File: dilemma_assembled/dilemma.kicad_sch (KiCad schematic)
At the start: 103 parts, among them J1 USB_C_Receptacle_USB2.0, J102 NA_serial, J105 NA_Conn_01x04_Female, J113 Cirque, J2 NA_Conn_01x03_Female, J5 Conn_01x02, SW1 SW_Push, SW101 NA_SW_Push, SW102 NA_SW_Push, SW103 NA_SW_Push, SW104 NA_SW_Push, SW105 NA_SW_Push, SW106 NA_SW_Push, SW107 NA_SW_Push, SW108 NA_SW_Push, SW109 NA_SW_Push, SW110 NA_SW_SPST, SW112 NA_SW_Push, SW113 NA_SW_Push, SW114 NA_SW_Push, SW115 NA_SW_Push, SW116 NA_SW_Push, SW117 NA_SW_Push, SW118 NA_SW_Push, SW119 NA_SW_Push, SW2 SW_Push, SW3001 NA_SW_Push, SW3002 NA_RotaryEncoder_Switch, U1 RP2040, U2 W25Q128JVS, U3 XC6210B332MR-G, U4 USBLC6-2P6, Y1 Crystal_GND24

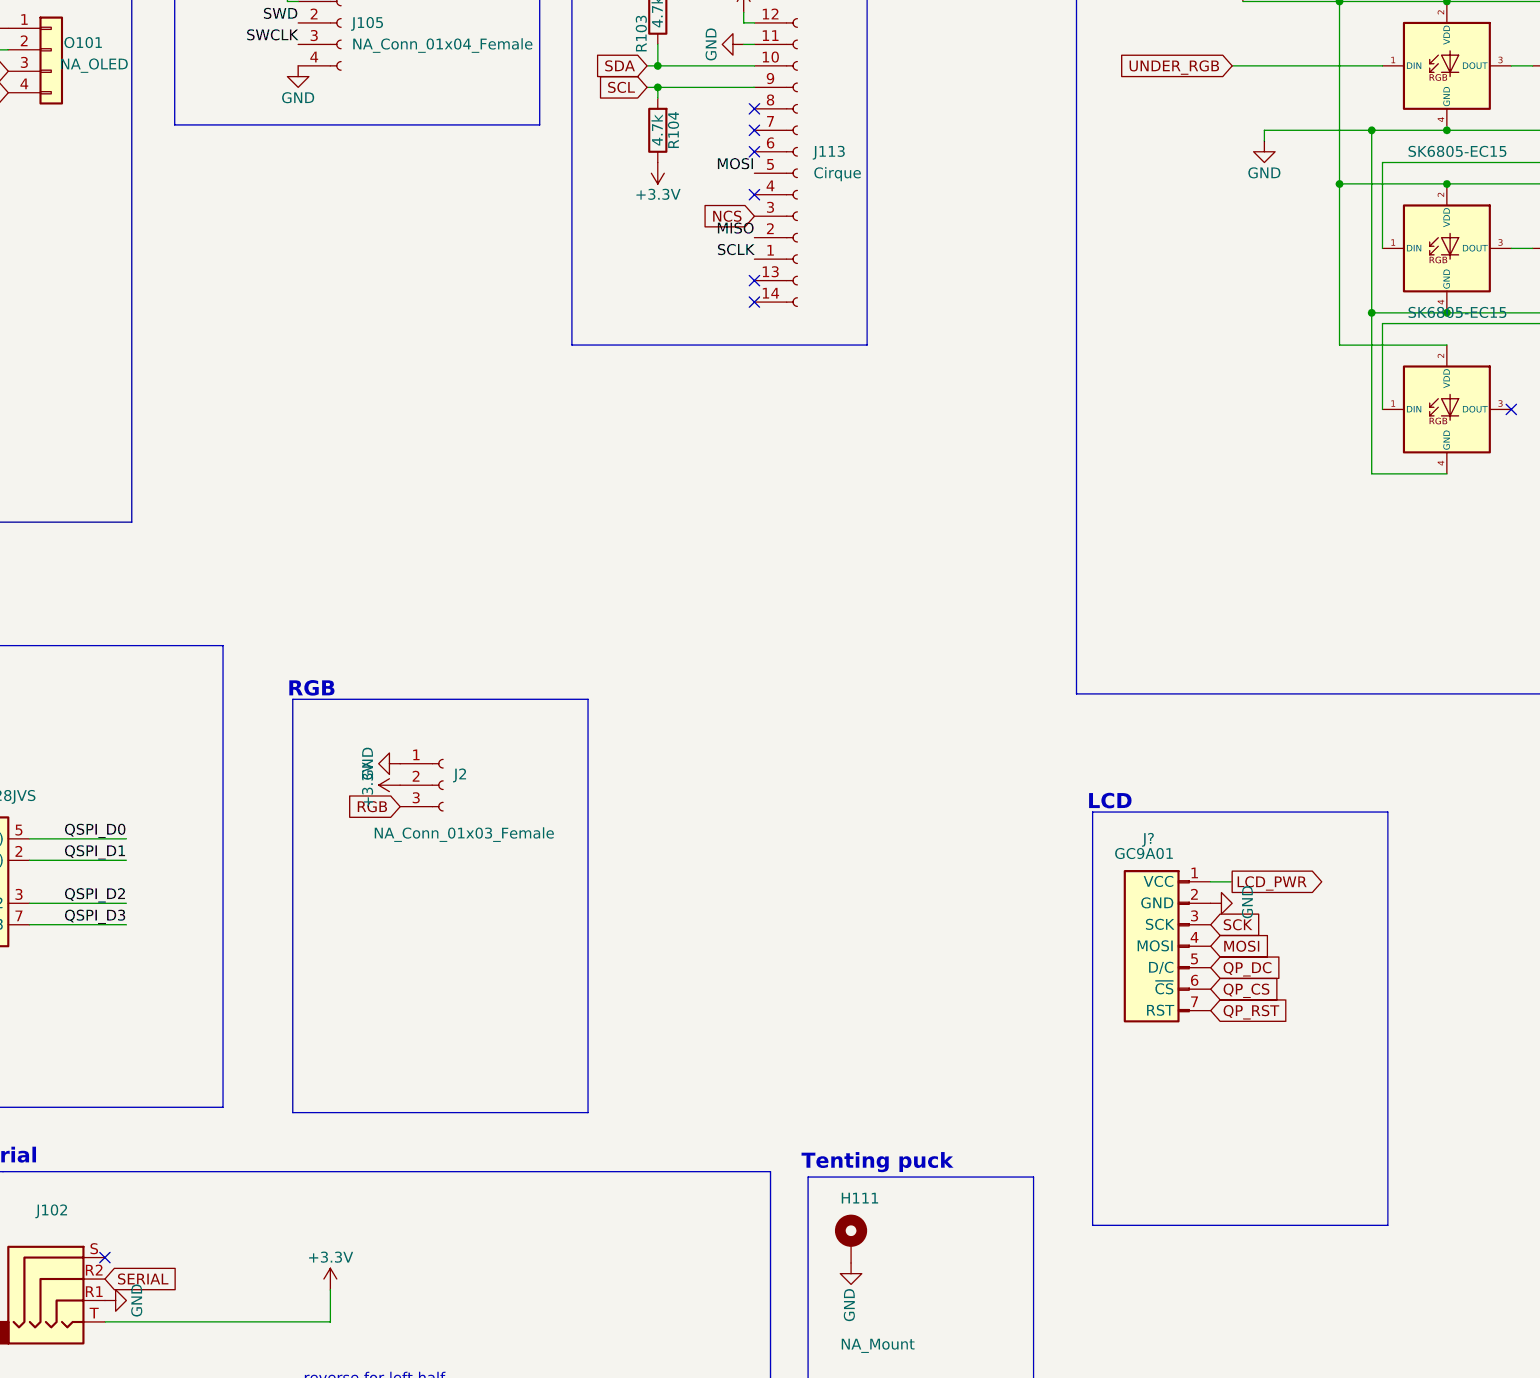
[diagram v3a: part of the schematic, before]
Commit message: add usb c cutout
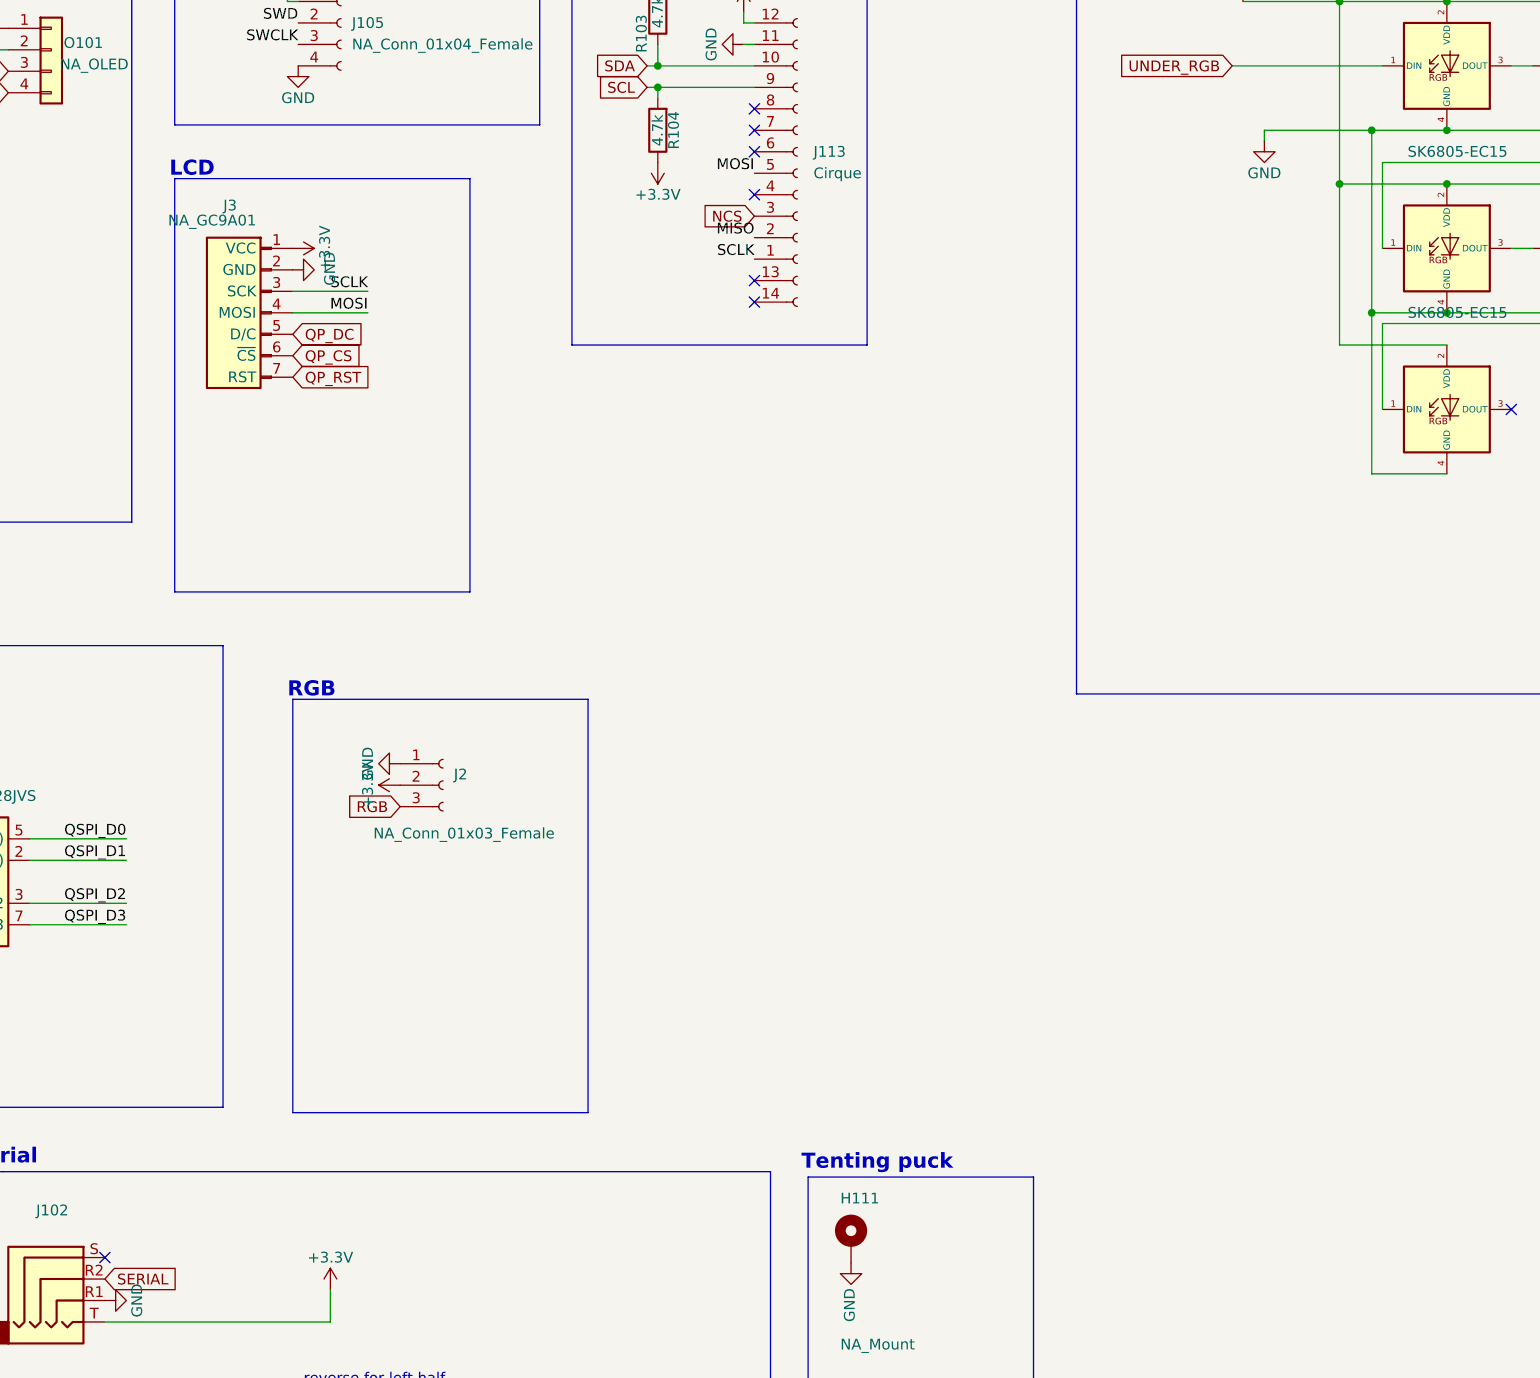
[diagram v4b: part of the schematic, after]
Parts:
- J3: renamed from J?; value GC9A01 -> NA_GC9A01; footprint prettylib:GC9A01-biggers hole -> Connector_PinHeader_2.54mm:PinHeader_1x07_P2.54mm_Vertical
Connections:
- net LCD_PWR is gone; now on net +3V3: J3.1 (VCC)
- net SCK is gone; now on net SCLK: J3.3 (SCK)
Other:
- moved on the sheet: J3
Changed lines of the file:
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@@
     (stroke (width 0) (type default) (color 0 0 0 0))
   )
-  (polyline (pts (xy 417.195 123.825) (xy 417.195 172.72))
+  (polyline (pts (xy 308.61 48.895) (xy 308.61 97.79))
     (stroke (width 0) (type default) (color 0 0 0 0))
   )
@@
     (stroke (width 0) (type default) (color 0 0 0 0))
   )
-  (wire (pts (xy 396.24 132.08) (xy 398.78 132.08))
-    (stroke (width 0) (type default) (color 0 0 0 0))
-  )
   (wire (pts (xy 64.135 44.45) (xy 64.135 45.085))
     (stroke (width 0) (type default) (color 0 0 0 0))
@@
     (stroke (width 0) (type default) (color 0 0 0 0))
   )
-  (polyline (pts (xy 382.27 123.825) (xy 382.27 172.72))
+  (polyline (pts (xy 273.685 48.895) (xy 273.685 97.79))
     (stroke (width 0) (type default) (color 0 0 0 0))
   )
@@
     (stroke (width 0) (type default) (color 0 0 0 0))
   )
-  (polyline (pts (xy 417.195 172.72) (xy 382.27 172.72))
+  (polyline (pts (xy 308.61 97.79) (xy 273.685 97.79))
     (stroke (width 0) (type default) (color 0 0 0 0))
   )
@@
     (stroke (width 0) (type default) (color 0 0 0 0))
   )
-  (polyline (pts (xy 382.27 123.825) (xy 417.195 123.825))
+  (polyline (pts (xy 273.685 48.895) (xy 308.61 48.895))
     (stroke (width 0) (type default) (color 0 0 0 0))
   )
@@
     (stroke (width 0) (type default) (color 0 0 0 0))
   )
+  (wire (pts (xy 287.655 64.77) (xy 296.545 64.77))
+    (stroke (width 0) (type default) (color 0 0 0 0))
+  )
   (wire (pts (xy 55.88 248.92) (xy 55.88 255.27))
     (stroke (width 0) (type default) (color 0 0 0 0))
@@
     (stroke (width 0) (type default) (color 0 0 0 0))
   )
+  (wire (pts (xy 287.655 62.23) (xy 296.545 62.23))
+    (stroke (width 0) (type default) (color 0 0 0 0))
+  )
   (polyline (pts (xy 250.19 210.185) (xy 299.72 210.185))
     (stroke (width 0) (type default) (color 0 0 0 0))
@@
     (effects (font (size 1.778 1.778) (thickness 0.3556) bold) (justify right bottom))
   )
-  (text "LCD" (at 381.635 123.825 0)
+  (text "LCD" (at 273.05 48.895 0)
     (effects (font (size 1.778 1.778) (thickness 0.3556) bold) (justify left bottom))
   )
@@
     (effects (font (size 1.27 1.27)) (justify left bottom))
   )
+  (label "SCLK" (at 296.545 62.23 180)
+    (effects (font (size 1.27 1.27)) (justify right bottom))
+  )
   (label "~{RESET}" (at 118.745 106.68 0)
     (effects (font (size 1.27 1.27)) (justify left bottom))
@@
     (effects (font (size 1.27 1.27)) (justify right bottom))
   )
+  (label "MOSI" (at 296.545 64.77 180)
+    (effects (font (size 1.27 1.27)) (justify right bottom))
+  )
   (label "QSPI_D1" (at 267.97 129.54 180)
     (effects (font (size 1.27 1.27)) (justify right bottom))
@@
     )
   )
-  (global_label "SCK" (shape input) (at 396.24 137.16 0) (fields_autoplaced)
-    (effects (font (size 1.27 1.27)) (justify left))
-    (property "Intersheet References" "${INTERSHEET_REFS}" (id 0) (at 402.4026 137.0806 0)
-      (effects (font (size 1.27 1.27)) (justify left) hide)
-    )
-  )
   (global_label "M_ROW3" (shape input) (at 33.02 226.06 180)
     (effects (font (size 1.27 1.27)) (justify right))
@@
     )
   )
-  (global_label "QP_RST" (shape input) (at 396.24 147.32 0) (fields_autoplaced)
+  (global_label "QP_RST" (shape input) (at 287.655 72.39 0) (fields_autoplaced)
     (effects (font (size 1.27 1.27)) (justify left))
-    (property "Intersheet References" "${INTERSHEET_REFS}" (id 0) (at 405.6683 147.2406 0)
+    (property "Intersheet References" "${INTERSHEET_REFS}" (id 0) (at 297.0833 72.3106 0)
       (effects (font (size 1.27 1.27)) (justify left) hide)
     )
@@
     )
   )
-  (global_label "QP_DC" (shape input) (at 396.24 142.24 0) (fields_autoplaced)
+  (global_label "QP_DC" (shape input) (at 287.655 67.31 0) (fields_autoplaced)
     (effects (font (size 1.27 1.27)) (justify left))
-    (property "Intersheet References" "${INTERSHEET_REFS}" (id 0) (at 404.7612 142.1606 0)
+    (property "Intersheet References" "${INTERSHEET_REFS}" (id 0) (at 296.1762 67.2306 0)
       (effects (font (size 1.27 1.27)) (justify left) hide)
     )
@@
     )
   )
-  (global_label "LCD_PWR" (shape output) (at 398.78 132.08 0) (fields_autoplaced)
-    (effects (font (size 1.27 1.27)) (justify left))
-    (property "Intersheet References" "${INTERSHEET_REFS}" (id 0) (at 129.54 -330.2 0)
-      (effects (font (size 1.27 1.27)) hide)
-    )
-  )
   (global_label "RGB" (shape input) (at 182.88 58.42 0)
     (effects (font (size 1.27 1.27)) (justify left))
@@
     )
   )
-  (global_label "QP_CS" (shape input) (at 396.24 144.78 0) (fields_autoplaced)
-    (effects (font (size 1.27 1.27)) (justify left))
-    (property "Intersheet References" "${INTERSHEET_REFS}" (id 0) (at 404.7007 144.7006 0)
-      (effects (font (size 1.27 1.27)) (justify left) hide)
-    )
-  )
-  (global_label "MOSI" (shape input) (at 396.24 139.7 0) (fields_autoplaced)
+  (global_label "QP_CS" (shape input) (at 287.655 69.85 0) (fields_autoplaced)
     (effects (font (size 1.27 1.27)) (justify left))
-    (property "Intersheet References" "${INTERSHEET_REFS}" (id 0) (at 403.2493 139.6206 0)
+    (property "Intersheet References" "${INTERSHEET_REFS}" (id 0) (at 296.1157 69.7706 0)
       (effects (font (size 1.27 1.27)) (justify left) hide)
     )
@@
     (pin "1")
   )
-  (symbol (lib_id "kbd:IPS_LCD__gc9a01_240X240") (at 392.43 139.7 0) (mirror y) (unit 1)
+  (symbol (lib_id "kbd:IPS_LCD__gc9a01_240X240") (at 283.845 64.77 0) (mirror y) (unit 1)
     (in_bom no) (on_board yes)
-    (property "Reference" "J?" (id 0) (at 389.636 127 0)
+    (property "Reference" "J3" (id 0) (at 281.051 52.07 0)
       (effects (font (size 1.27 1.27)) (justify left))
     )
-    (property "Value" "GC9A01" (id 1) (at 391.922 128.778 0)
+    (property "Value" "NA_GC9A01" (id 1) (at 283.337 53.848 0)
       (effects (font (size 1.27 1.27)) (justify left))
     )
-    (property "Footprint" "prettylib:GC9A01-biggers hole" (id 2) (at 391.16 124.46 0)
+    (property "Footprint" "Connector_PinHeader_2.54mm:PinHeader_1x07_P2.54mm_Vertical" (id 2) (at 282.575 49.53 0)
       (effects (font (size 1.27 1.27)) hide)
     )
-    (property "Datasheet" "~" (id 3) (at 391.16 124.46 0)
+    (property "Datasheet" "~" (id 3) (at 282.575 49.53 0)
       (effects (font (size 1.27 1.27)) hide)
     )
@@
     (pin "7")
   )
+  (symbol (lib_id "power:+3.3V") (at 287.655 57.15 270) (unit 1)
+    (in_bom yes) (on_board yes)
+    (property "Reference" "#PWR0109" (id 0) (at 283.845 57.15 0)
+      (effects (font (size 1.27 1.27)) hide)
+    )
+    (property "Value" "+3.3V" (id 1) (at 291.465 57.15 0))
+    (property "Footprint" "" (id 2) (at 287.655 57.15 0)
+      (effects (font (size 1.27 1.27)) hide)
+    )
+    (property "Datasheet" "" (id 3) (at 287.655 57.15 0)
+      (effects (font (size 1.27 1.27)) hide)
+    )
+    (pin "1")
+  )
   (symbol (lib_id "Device:C") (at 91.44 180.34 0) (unit 1)
     (in_bom yes) (on_board yes)
@@
     (pin "1")
   )
-  (symbol (lib_id "power:GND") (at 396.24 134.62 90) (unit 1)
+  (symbol (lib_id "power:GND") (at 287.655 59.69 90) (unit 1)
     (in_bom yes) (on_board yes)
-    (property "Reference" "#PWR?" (id 0) (at 402.59 134.62 0)
+    (property "Reference" "#PWR0106" (id 0) (at 294.005 59.69 0)
       (effects (font (size 1.27 1.27)) hide)
     )
-    (property "Value" "GND" (id 1) (at 400.6342 134.493 0))
-    (property "Footprint" "" (id 2) (at 396.24 134.62 0)
+    (property "Value" "GND" (id 1) (at 292.0492 59.563 0))
+    (property "Footprint" "" (id 2) (at 287.655 59.69 0)
       (effects (font (size 1.27 1.27)) hide)
     )
-    (property "Datasheet" "" (id 3) (at 396.24 134.62 0)
+    (property "Datasheet" "" (id 3) (at 287.655 59.69 0)
       (effects (font (size 1.27 1.27)) hide)
     )
@@
       (reference "#PWR0105") (unit 1) (value "+3.3V") (footprint "")
     )
+    (path "/f1f8c5e8-84ec-46cc-976a-c595f2716600"
+      (reference "#PWR0106") (unit 1) (value "GND") (footprint "")
+    )
     (path "/d8004053-a96a-4db9-be88-aefe8064c65c"
       (reference "#PWR0107") (unit 1) (value "GND") (footprint "")
@@
       (reference "#PWR0108") (unit 1) (value "GND") (footprint "")
     )
+    (path "/6e8f654f-3f23-4336-af6c-2b78ed5fcffb"
+      (reference "#PWR0109") (unit 1) (value "+3.3V") (footprint "")
+    )
     (path "/9c465d0a-3acf-44e4-926b-a8e6ae8ccd7b"
       (reference "#PWR0110") (unit 1) (value "GND") (footprint "")
@@
       (reference "#PWR0132") (unit 1) (value "+3.3V") (footprint "")
     )
-    (path "/f1f8c5e8-84ec-46cc-976a-c595f2716600"
-      (reference "#PWR?") (unit 1) (value "GND") (footprint "")
-    )
     (path "/4a21e78b-0ab0-4b88-8132-9b174e045719"
       (reference "C1") (unit 1) (value "1µ") (footprint "Capacitor_SMD:C_0603_1608Metric")
@@
       (reference "J2") (unit 1) (value "NA_Conn_01x03_Female") (footprint "local-libraries:PinHeader_1x03_P2.54mm_Vertical_smd")
     )
+    (path "/6e2411cd-fd67-4be2-b1a3-b3e54de4894a"
+      (reference "J3") (unit 1) (value "NA_GC9A01") (footprint "Connector_PinHeader_2.54mm:PinHeader_1x07_P2.54mm_Vertical")
+    )
     (path "/06b6e523-10ae-4799-8871-3c7a3a700ad9"
       (reference "J5") (unit 1) (value "Conn_01x02") (footprint "Connector_PinHeader_1.27mm:PinHeader_1x02_P1.27mm_Vertical")
@@
       (reference "J113") (unit 1) (value "Cirque") (footprint "local-libraries:FPC-SMD_FPC05012-09200-.5mm")
     )
-    (path "/6e2411cd-fd67-4be2-b1a3-b3e54de4894a"
-      (reference "J?") (unit 1) (value "GC9A01") (footprint "prettylib:GC9A01-biggers hole")
-    )
     (path "/66096f4f-c798-4425-8537-e7adeb21bec3"
       (reference "O101") (unit 1) (value "NA_OLED") (footprint "local-libraries:PinHeader_1x04_P2.54mm_Vertical")
@@
       (reference "U1") (unit 1) (value "RP2040") (footprint "0xLib_Package_DFN_QFN:QFN-56-1EP_7x7mm_P0.4mm_EP3.2x3.2mm")
     )
-    (path "/f05b539d-f3ed-4d87-8562-322d3113dab5"
+    (path "/f05b539d-f3ed-4d87-8562-322d3113dab6"
       (reference "U2") (unit 1) (value "W25Q128JVS") (footprint "drawings:W25Q128JVPIQ")
     )

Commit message: routing
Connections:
- net QP_CS: now also U1.15 (GPIO12)
- net QP_DC: now also U1.14 (GPIO11)
- net QP_RST: now also U1.16 (GPIO13)
- no-connect marks 19 -> 16
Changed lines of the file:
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@@
   (no_connect (at 182.88 121.92))
   (no_connect (at 182.88 104.14))
-  (no_connect (at 182.88 86.36))
   (no_connect (at 265.43 176.53))
   (no_connect (at 50.8 64.77))
   (no_connect (at 50.8 67.31))
   (no_connect (at 342.265 45.72))
-  (no_connect (at 182.88 88.9))
-  (no_connect (at 182.88 91.44))
   (no_connect (at 182.88 93.98))
   (no_connect (at 182.88 96.52))
@@
     )
   )
+  (global_label "QP_CS" (shape input) (at 182.88 88.9 0) (fields_autoplaced)
+    (effects (font (size 1.27 1.27)) (justify left))
+    (property "Intersheet References" "${INTERSHEET_REFS}" (id 0) (at 191.3407 88.8206 0)
+      (effects (font (size 1.27 1.27)) (justify left) hide)
+    )
+  )
   (global_label "M_ROW3" (shape input) (at 182.88 71.12 0)
     (effects (font (size 1.27 1.27)) (justify left))
@@
     )
   )
+  (global_label "QP_RST" (shape input) (at 182.88 91.44 0) (fields_autoplaced)
+    (effects (font (size 1.27 1.27)) (justify left))
+    (property "Intersheet References" "${INTERSHEET_REFS}" (id 0) (at 192.3083 91.3606 0)
+      (effects (font (size 1.27 1.27)) (justify left) hide)
+    )
+  )
   (global_label "M_COL2" (shape input) (at 93.98 213.36 90)
     (effects (font (size 1.27 1.27)) (justify left))
@@
     )
   )
+  (global_label "QP_DC" (shape input) (at 182.88 86.36 0) (fields_autoplaced)
+    (effects (font (size 1.27 1.27)) (justify left))
+    (property "Intersheet References" "${INTERSHEET_REFS}" (id 0) (at 191.4012 86.2806 0)
+      (effects (font (size 1.27 1.27)) (justify left) hide)
+    )
+  )

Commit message: bom
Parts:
- J5: value Conn_01x02 -> NA_Conn_01x02
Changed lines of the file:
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@@
       (effects (font (size 1.27 1.27)) (justify left))
     )
-    (property "Value" "Conn_01x02" (id 1) (at 72.39 172.0851 0)
+    (property "Value" "NA_Conn_01x02" (id 1) (at 72.39 172.0851 0)
       (effects (font (size 1.27 1.27)) (justify left) hide)
     )
@@
     )
     (path "/06b6e523-10ae-4799-8871-3c7a3a700ad9"
-      (reference "J5") (unit 1) (value "Conn_01x02") (footprint "Connector_PinHeader_1.27mm:PinHeader_1x02_P1.27mm_Vertical")
+      (reference "J5") (unit 1) (value "NA_Conn_01x02") (footprint "Connector_PinHeader_1.27mm:PinHeader_1x02_P1.27mm_Vertical")
     )
     (path "/348a0c3a-4854-4149-8a7a-ae4295b639cb"

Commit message: fix per key RGB connection
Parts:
- J3: footprint Connector_PinHeader_2.54mm:PinHeader_1x07_P2.54mm_Vertical -> local-libraries:PinHeader_1x07_P2.54mm_Vertical
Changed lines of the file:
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@@
       (effects (font (size 1.27 1.27)) (justify left))
     )
-    (property "Footprint" "Connector_PinHeader_2.54mm:PinHeader_1x07_P2.54mm_Vertical" (id 2) (at 282.575 49.53 0)
+    (property "Footprint" "local-libraries:PinHeader_1x07_P2.54mm_Vertical" (id 2) (at 282.575 49.53 0)
       (effects (font (size 1.27 1.27)) hide)
     )
@@
     )
     (path "/6e2411cd-fd67-4be2-b1a3-b3e54de4894a"
-      (reference "J3") (unit 1) (value "NA_GC9A01") (footprint "Connector_PinHeader_2.54mm:PinHeader_1x07_P2.54mm_Vertical")
+      (reference "J3") (unit 1) (value "NA_GC9A01") (footprint "local-libraries:PinHeader_1x07_P2.54mm_Vertical")
     )
     (path "/06b6e523-10ae-4799-8871-3c7a3a700ad9"

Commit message: connect rotary encoder pins
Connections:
- net ENC_PIN1: now also U1.36 (GPIO24)
- net ENC_PIN2: now also U1.37 (GPIO25)
- no-connect marks 16 -> 14
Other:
- note added: "Underglow RGB"
- moved on the sheet: D11, D12, D15, D16, D18, D19, D21, D22, D24, D25, D27, D28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
